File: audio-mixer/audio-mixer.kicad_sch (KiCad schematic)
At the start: 52 parts, among them J1 Input A1, J10 Pot, J11 Input B3, J12 Pot, J13 Pot, J14 Output A, J15 Pot, J16 Output B, J17 AudioJack4, J18 Power, J19 Power, J2 Pot, J20 Power, J3 Input A2, J4 Pot, J5 Input A3, J6 Pot, J7 Input B1, J8 Pot, J9 Input B2, SW1 Mono/Stereo, U1 TL074

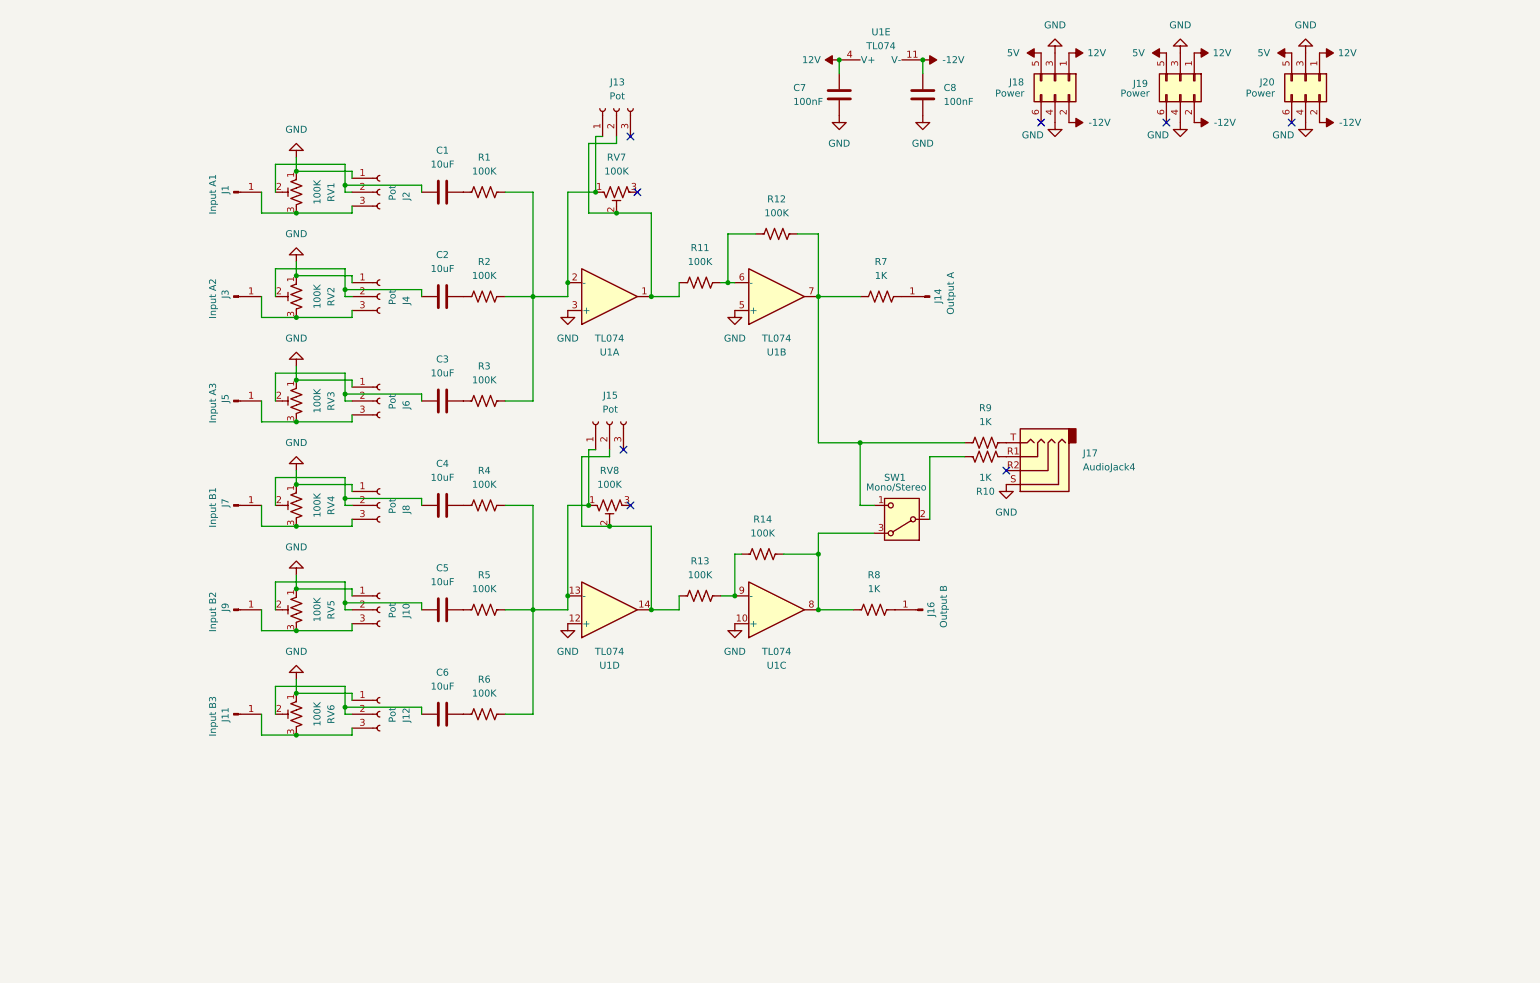
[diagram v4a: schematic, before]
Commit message: Update audio mixer to new format
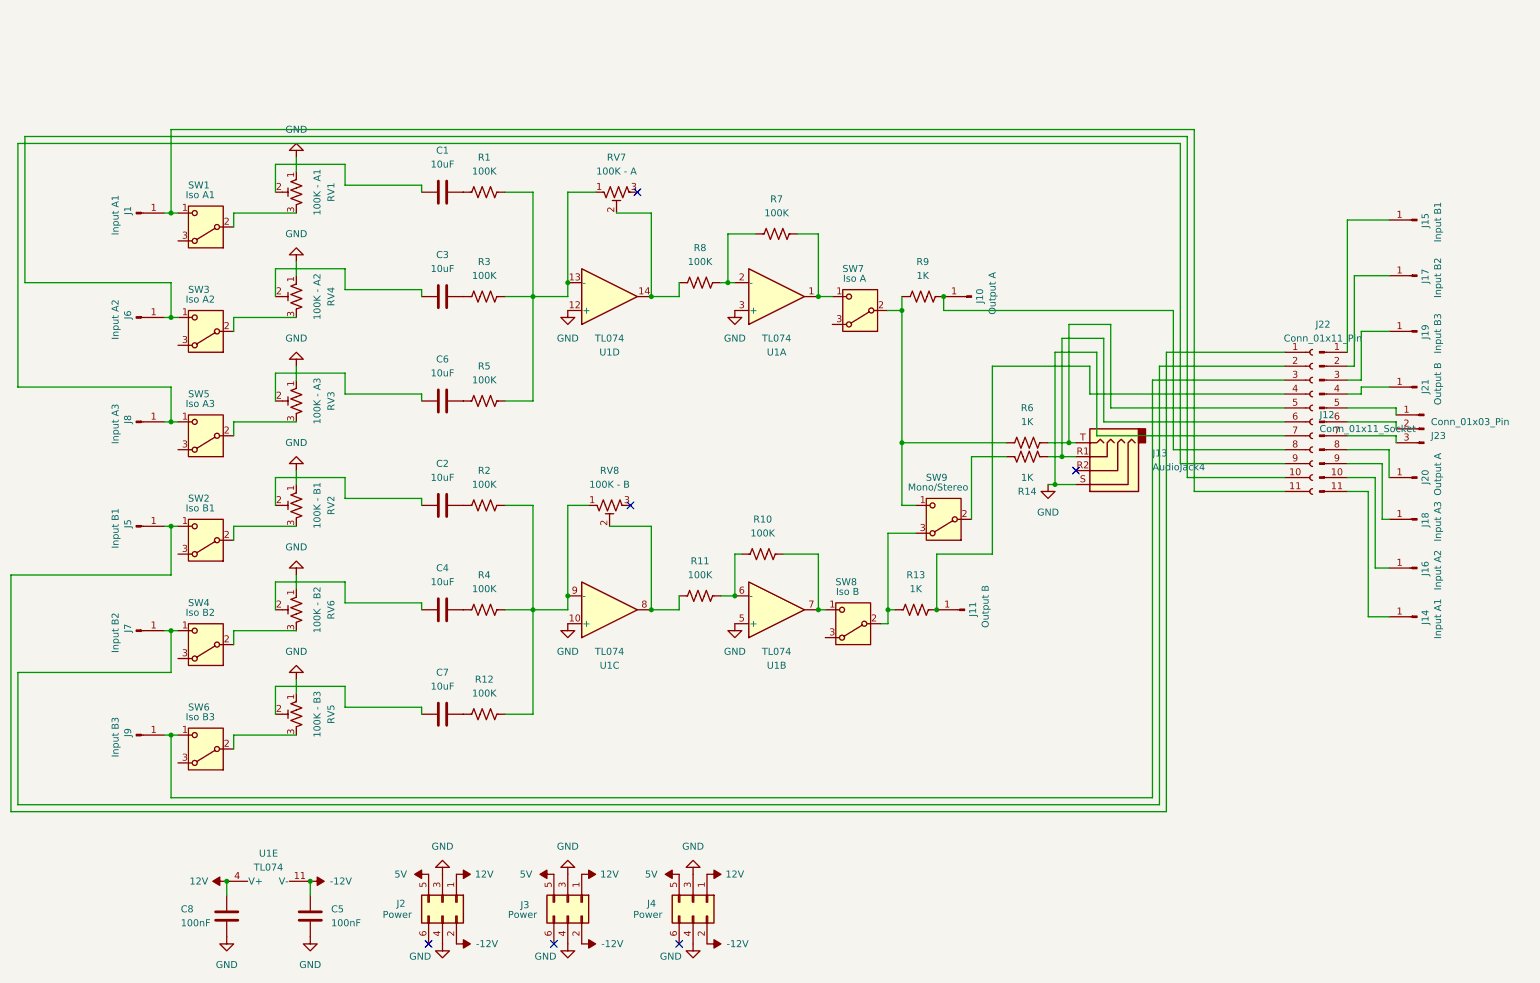
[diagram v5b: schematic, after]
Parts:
- removed J10, J12, J13, J15, J2, J4, J6, J8: Pot, modular2:pot, symbol Connector:Conn_01x03_Socket
- added J12: Conn_01x11_Socket, Connector_PinSocket_2.54mm:PinSocket_1x11_P2.54mm_Vertical, symbol Connector:Conn_01x11_Socket
- added J14: Input A1, modular2:banana-jack, symbol Connector:Conn_01x01_Pin
- added J15: Input B1, modular2:banana-jack, symbol Connector:Conn_01x01_Pin
- added J16: Input A2, modular2:banana-jack, symbol Connector:Conn_01x01_Pin
- added J17: Input B2, modular2:banana-jack, symbol Connector:Conn_01x01_Pin
- added J18: Input A3, modular2:banana-jack, symbol Connector:Conn_01x01_Pin
- added J19: Input B3, modular2:banana-jack, symbol Connector:Conn_01x01_Pin
- added J20: Output A, modular2:banana-jack, symbol Connector:Conn_01x01_Pin
- added J21: Output B, modular2:banana-jack, symbol Connector:Conn_01x01_Pin
- added J22: Conn_01x11_Pin, Connector_PinHeader_2.54mm:PinHeader_1x11_P2.54mm_Vertical, symbol Connector:Conn_01x11_Pin
- added J23: Conn_01x03_Pin, Connector_PinHeader_2.54mm:PinHeader_1x03_P2.54mm_Vertical, symbol Connector:Conn_01x03_Pin
- added SW1: Iso A1, modular2:switch1, symbol Switch:SW_Nidec_CAS-120A1
- added SW2: Iso B1, modular2:switch1, symbol Switch:SW_Nidec_CAS-120A1
- added SW3: Iso A2, modular2:switch1, symbol Switch:SW_Nidec_CAS-120A1
- added SW4: Iso B2, modular2:switch1, symbol Switch:SW_Nidec_CAS-120A1
- added SW5: Iso A3, modular2:switch1, symbol Switch:SW_Nidec_CAS-120A1
- added SW6: Iso B3, modular2:switch1, symbol Switch:SW_Nidec_CAS-120A1
- added SW7: Iso A, modular2:switch1, symbol Switch:SW_Nidec_CAS-120A1
- added SW8: Iso B, modular2:switch1, symbol Switch:SW_Nidec_CAS-120A1
- RV1: value 100K -> 100K - A1; footprint modular2:pot-socket -> modular2:Potentiometer_Alps_RK09K_Single_Vertical - knob padding
- RV2: renamed from RV4; value 100K -> 100K - B1; footprint modular2:pot-socket -> modular2:Potentiometer_Alps_RK09K_Single_Vertical - knob padding
- RV3: value 100K -> 100K - A3; footprint modular2:pot-socket -> modular2:Potentiometer_Alps_RK09K_Single_Vertical - knob padding
- RV4: renamed from RV2; value 100K -> 100K - A2; footprint modular2:pot-socket -> modular2:Potentiometer_Alps_RK09K_Single_Vertical - knob padding
- RV5: renamed from RV6; value 100K -> 100K - B3; footprint modular2:pot-socket -> modular2:Potentiometer_Alps_RK09K_Single_Vertical - knob padding
- RV6: renamed from RV5; value 100K -> 100K - B2; footprint modular2:pot-socket -> modular2:Potentiometer_Alps_RK09K_Single_Vertical - knob padding
- RV7: value 100K -> 100K - A; footprint modular2:pot-socket -> modular2:Potentiometer_Alps_RK09K_Single_Vertical - knob padding
- RV8: value 100K -> 100K - B; footprint modular2:pot-socket -> modular2:Potentiometer_Alps_RK09K_Single_Vertical - knob padding
- renumbered C4 to C2, C2 to C3, C5 to C4, C8 to C5, C3 to C6, C6 to C7, C7 to C8, J14 to J10, J16 to J11, J17 to J13, J18 to J2, J19 to J3, J20 to J4, J7 to J5, J3 to J6, J9 to J7, J5 to J8, J11 to J9, R14 to R10, R13 to R11, R6 to R12, R8 to R13, R10 to R14, R4 to R2, R2 to R3, R5 to R4, R3 to R5, R9 to R6, R12 to R7, R11 to R8, R7 to R9, SW1 to SW9
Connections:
- net GND: now also J12.7 (Pin_7)
- net at RV1.3: now also SW1.2 (B); no longer J1.1 (Pin_1)
- net at R1.2, R3.2, R5.2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: now also U1.13 (-); no longer U1.2 (-)
- net at R7.1, R8.2: now also U1.2 (-); no longer U1.6 (-)
- net at R6.1, R9.1, SW9.1 (C): now also SW7.2 (B); no longer R7.2, U1.7
- net at RV4.3: now also SW3.2 (B); no longer J6.1 (Pin_1)
- net at R10.1, R11.2: now also U1.6 (-); no longer U1.9 (-)
- net at R13.1, SW9.3 (A): now also SW8.2 (B); no longer R10.2, U1.8
- net at J8.1 (Pin_1): now also J12.9 (Pin_9), SW5.1 (C); no longer RV3.3
- net at J5.1 (Pin_1): now also J12.1 (Pin_1), SW2.1 (C); no longer RV2.3
- net at J7.1 (Pin_1): now also J12.2 (Pin_2), SW4.1 (C); no longer RV6.3
- net at R11.1, RV8.2: now also U1.8; no longer U1.14
- net at J9.1 (Pin_1): now also J12.3 (Pin_3), SW6.1 (C); no longer RV5.3
- net at R12.2, R2.2, R4.2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: now also U1.9 (-); no longer U1.13 (-)
- net at J10.1 (Pin_1), R9.2: now also J12.8 (Pin_8)
- net at J13.R1, R14.2: now also J12.6 (Pin_6)
- net at J13.T, R6.2: now also J12.5 (Pin_5)
- net at R8.1, RV7.2: now also U1.14; no longer U1.1
- net at J11.1 (Pin_1), R13.2: now also J12.4 (Pin_4)
- new net: J14.1 (Pin_1), J22.11 (Pin_11)
- new net: R7.2, SW7.1 (C), U1.1
- new net: RV5.3, SW6.2 (B)
- new net: J22.5 (Pin_5), J23.1 (Pin_1)
- new net: J22.6 (Pin_6), J23.2 (Pin_2)
- new net: J22.7 (Pin_7), J23.3 (Pin_3)
- new net: R10.2, SW8.1 (C), U1.7
- new net: RV3.3, SW5.2 (B)
- new net: J12.10 (Pin_10), J6.1 (Pin_1), SW3.1 (C)
- new net: J1.1 (Pin_1), J12.11 (Pin_11), SW1.1 (C)
- new net: J15.1 (Pin_1), J22.1 (Pin_1)
- new net: J16.1 (Pin_1), J22.10 (Pin_10)
- new net: J17.1 (Pin_1), J22.2 (Pin_2)
- new net: J19.1 (Pin_1), J22.3 (Pin_3)
- new net: J21.1 (Pin_1), J22.4 (Pin_4)
- new net: J20.1 (Pin_1), J22.8 (Pin_8)
- new net: J18.1 (Pin_1), J22.9 (Pin_9)
- new net: RV6.3, SW4.2 (B)
- new net: RV2.3, SW2.2 (B)
- no-connect marks 8 -> 6
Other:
- moved on the sheet: C5, C8, J1, J10, J11, J13, J2, J3, J4, J5, J6, J7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
